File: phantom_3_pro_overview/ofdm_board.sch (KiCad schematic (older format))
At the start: 0 parts

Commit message: Overview: Conceptual schematics of some components.
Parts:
- added U?: STM32F 103CBU6, ARM Cortex-M3 MCU, symbol IC_PQFP32
- added U?: AD9363, RF 2x2 transceiver, symbol IC_PQFP32
- added U?: 5CEFA4U19I7, Altera Cyclone V FPGA, symbol IC_PQFP32
- added U?: CY7C68013A, Hi-Speed USB Ctrl., symbol CY7C420
- added U?: MGA-22003, 2.3-2.7 GHz Pwr Amp, symbol AMP
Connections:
- net labels added: GND, VCC
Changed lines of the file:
@@
 LIBS:valves
 LIBS:motors
+LIBS:ic_dil_generic
+LIBS:sensors
+LIBS:u-blox
+LIBS:amplifiers
 LIBS:phantom_3_pro_overview-cache
 EELAYER 25 0
@@
 encoding utf-8
 Sheet 2 23
-Title ""
+Title "Overview of the Phantom 3 Pro OFDM board"
 Date ""
 Rev ""
 Comp ""
-Comment1 ""
+Comment1 "This schematic does not aim to be electrically correct, it is conceptual."
 Comment2 ""
 Comment3 ""
@@
 RIB_OFDM
 Wire Bus Line
-	3100 2450 3600 2450
-Text HLabel 3600 2450 2    60   BiDi ~ 0
+	8500 1850 9000 1850
+Text HLabel 9000 1850 2    60   BiDi ~ 0
 ANTENNA1
 Wire Bus Line
-	3100 2700 3600 2700
-Text HLabel 3600 2700 2    60   BiDi ~ 0
+	8500 2100 9000 2100
+Text HLabel 9000 2100 2    60   BiDi ~ 0
 ANTENNA2
 Wire Bus Line
-	3150 2900 3650 2900
-Text HLabel 3650 2900 2    60   BiDi ~ 0
+	8550 2300 9050 2300
+Text HLabel 9050 2300 2    60   BiDi ~ 0
 ANTENNA3
 Wire Bus Line
-	3150 3100 3650 3100
-Text HLabel 3650 3100 2    60   BiDi ~ 0
+	8550 2500 9050 2500
+Text HLabel 9050 2500 2    60   BiDi ~ 0
 ANTENNA4
+$Comp
+L IC_PQFP32 U?
+U 1 1 596EF58E
+P 4050 3650
+F 0 "U?" H 4050 3550 50  0001 C CNN
+F 1 "STM32F 103CBU6" H 4050 3750 50  0000 C CNN
+F 2 "ARM Cortex-M3 MCU" H 4050 3650 50  0000 C CNN
+F 3 "DOCUMENTATION" H 4050 3650 50  0001 C CNN
+	1    4050 3650
+	1    0    0    -1
+$EndComp
+$Comp
+L IC_PQFP32 U?
+U 1 1 596EF5FD
+P 6500 2150
+F 0 "U?" H 6500 2050 50  0001 C CNN
+F 1 "AD9363" H 6500 2250 50  0000 C CNN
+F 2 "RF 2x2 transceiver" H 6500 2150 50  0000 C CNN
+F 3 "DOCUMENTATION" H 6500 2150 50  0001 C CNN
+	1    6500 2150
+	1    0    0    -1
+$EndComp
+$Comp
+L IC_PQFP32 U?
+U 1 1 596EF87B
+P 8200 4850
+F 0 "U?" H 8200 4750 50  0001 C CNN
+F 1 "5CEFA4U19I7" H 8200 4950 50  0000 C CNN
+F 2 "Altera Cyclone V FPGA" H 8200 4850 50  0000 C CNN
+F 3 "DOCUMENTATION" H 8200 4850 50  0001 C CNN
+	1    8200 4850
+	1    0    0    -1
+$EndComp
+$Comp
+L CY7C420 U?
+U 1 1 596EFA52
+P 2050 4250
+F 0 "U?" H 1500 5150 50  0001 L CNN
+F 1 "CY7C68013A" H 2350 5150 50  0000 L CNN
+F 2 "Hi-Speed USB Ctrl." H 2050 4250 50  0000 C CNN
+F 3 "" H 2050 4250 50  0001 C CNN
+	1    2050 4250
+	1    0    0    -1
+$EndComp
+$Comp
+L AMP U?
+U 1 1 596EFDFE
+P 7900 1850
+F 0 "U?" H 8150 1950 50  0001 C CNN
+F 1 "MGA-22003" H 8000 1750 50  0000 C CNN
+F 2 "2.3-2.7 GHz Pwr Amp" H 8100 1700 50  0000 C CNN
+F 3 "" H 7900 1850 50  0001 C CNN
+	1    7900 1850
+	1    0    0    -1
+$EndComp
+$Comp
+L VCC #PWR?
+U 1 1 596F00EB
+P 7800 1550
+F 0 "#PWR?" H 7800 1400 50  0001 C CNN
+F 1 "VCC" H 7800 1700 50  0000 C CNN
+F 2 "" H 7800 1550 50  0001 C CNN
+F 3 "" H 7800 1550 50  0001 C CNN
+	1    7800 1550
+	1    0    0    -1
+$EndComp
+$Comp
+L GND #PWR?
+U 1 1 596F00FF
+P 7800 2150
+F 0 "#PWR?" H 7800 1900 50  0001 C CNN
+F 1 "GND" H 7800 2000 50  0000 C CNN
+F 2 "" H 7800 2150 50  0001 C CNN
+F 3 "" H 7800 2150 50  0001 C CNN
+	1    7800 2150
+	1    0    0    -1
+$EndComp
 $EndSCHEMATC

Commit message: Overview: Added OFDM board.
Besides drawing the OFDM, components were updated.
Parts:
- removed U?: 5CEFA4U19I7, Altera Cyclone V FPGA, symbol IC_PQFP32
- removed U?: CY7C68013A, Hi-Speed USB Ctrl., symbol CY7C420
- added U? (x2): S20, Rx_Tx_switch, symbol S20
- added U? (x2): TQP3M9037, Low Noise Amp, symbol AMP
- added U? (x2): S20, Ant_select, symbol S20
- added U?: MGA-22003, 2.3-2.7 GHz Pwr Amp, symbol AMP
- added U?: CY7C68013A, Hi-Speed, symbol IC_DIL16
- added U?: 5CEFA4U19I7, Altera Cyclone V FPGA, symbol IC_PQFP48
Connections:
- wire segments 0 -> 158

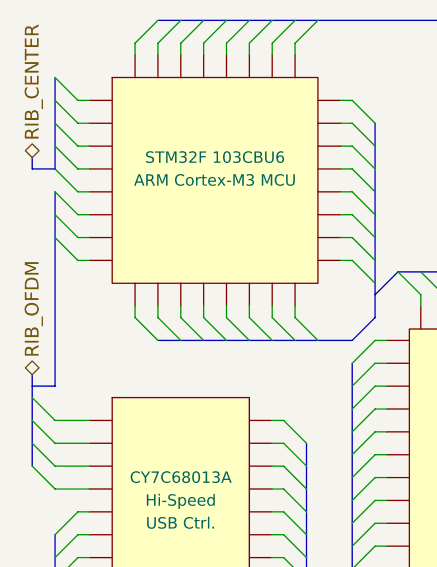
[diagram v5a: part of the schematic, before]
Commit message: Overview: Updated to latest findings.
Added magnetometer to gimbal control, and made some minor fixes.
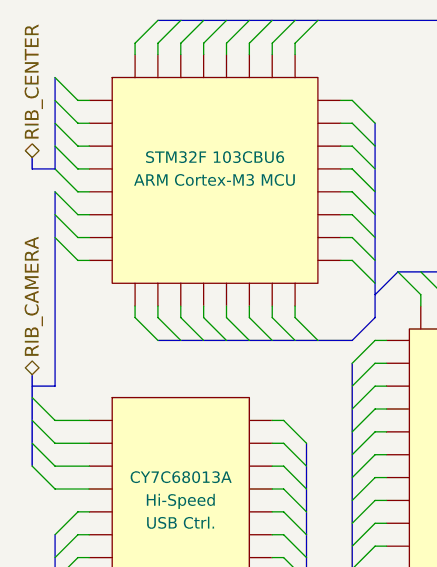
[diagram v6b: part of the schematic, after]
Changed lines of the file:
@@
 RIB_CENTER
 Text HLabel 600  2150 1    60   BiDi ~ 0
-RIB_OFDM
+RIB_CAMERA
 Text HLabel 8350 1900 2    60   BiDi ~ 0
 ANTENNA1

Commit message: Overview: Upgraded to KiCAD 5.0.1.
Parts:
- U? (x2): symbol IC_PQFP32 -> ic_dil_generic:IC_PQFP32
- U? (x4): symbol AMP -> amplifiers:AMP
- U? (x4): symbol S20 -> transistors-switches:S20
- U?: symbol IC_DIL16 -> ic_dil_generic:IC_DIL16
- U?: symbol IC_PQFP48 -> ic_dil_generic:IC_PQFP48
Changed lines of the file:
@@
-EESchema Schematic File Version 2
-LIBS:power
-LIBS:device
-LIBS:transistors
-LIBS:conn
-LIBS:linear
-LIBS:regul
-LIBS:74xx
-LIBS:cmos4000
-LIBS:adc-dac
-LIBS:memory
-LIBS:xilinx
-LIBS:microcontrollers
-LIBS:dsp
-LIBS:microchip
-LIBS:analog_switches
-LIBS:motorola
-LIBS:texas
-LIBS:intel
-LIBS:audio
-LIBS:interface
-LIBS:digital-audio
-LIBS:philips
-LIBS:display
-LIBS:cypress
-LIBS:siliconi
-LIBS:opto
-LIBS:atmel
-LIBS:contrib
-LIBS:valves
-LIBS:motors
-LIBS:ic_dil_generic
-LIBS:sensors
-LIBS:u-blox
-LIBS:amplifiers
-LIBS:transistors-switches
-LIBS:transistors-power
-LIBS:sensors-v2
-LIBS:regul-v2
+EESchema Schematic File Version 4
 LIBS:phantom_3_pro_overview-cache
-EELAYER 25 0
+EELAYER 26 0
 EELAYER END
 $Descr User 9449 5276
@@
 ANTENNA4
 $Comp
-L IC_PQFP32 U?
+L ic_dil_generic:IC_PQFP32 U?
 U 1 1 596EF58E
 P 1400 1300
@@
 $EndComp
 $Comp
-L IC_PQFP32 U?
+L ic_dil_generic:IC_PQFP32 U?
 U 1 1 596EF5FD
 P 4600 2700
@@
 $EndComp
 $Comp
-L AMP U?
+L amplifiers:AMP U?
 U 1 1 596EFDFE
 P 6350 1500
@@
 $EndComp
 $Comp
-L VCC #PWR?
+L power:VCC #PWR?
 U 1 1 596F00EB
 P 6250 1200
@@
 $EndComp
 $Comp
-L GND #PWR?
+L power:GND #PWR?
 U 1 1 596F00FF
 P 6250 1800
@@
 $EndComp
 $Comp
-L S20 U?
+L transistors-switches:S20 U?
 U 1 1 596FC8A9
 P 6950 2000
@@
 $EndComp
 $Comp
-L AMP U?
+L amplifiers:AMP U?
 U 1 1 596FC948
 P 5950 2000
@@
 $EndComp
 $Comp
-L VCC #PWR?
+L power:VCC #PWR?
 U 1 1 596FC94E
 P 6050 1700
@@
 $EndComp
 $Comp
-L GND #PWR?
+L power:GND #PWR?
 U 1 1 596FC954
 P 6050 2300
@@
 $EndComp
 $Comp
-L S20 U?
+L transistors-switches:S20 U?
 U 1 1 596FCA38
 P 7700 2000
@@
 $EndComp
 $Comp
-L VCC #PWR?
+L power:VCC #PWR?
 U 1 1 596FCA54
 P 6650 2300
@@
 $EndComp
 $Comp
-L VCC #PWR?
+L power:VCC #PWR?
 U 1 1 596FCA5F
 P 7700 1700
@@
 $EndComp
 $Comp
-L GND #PWR?
+L power:GND #PWR?
 U 1 1 596FCA6A
 P 7050 1600
@@
 $EndComp
 $Comp
-L GND #PWR?
+L power:GND #PWR?
 U 1 1 596FCA75
 P 7700 2300
@@
 	8050 2100 8150 2200
 $Comp
-L GND #PWR?
+L power:GND #PWR?
 U 1 1 596FCB1A
 P 8300 2000
@@
 	8150 2100 8250 2200
 $Comp
-L AMP U?
+L amplifiers:AMP U?
 U 1 1 596FD101
 P 6350 2550
@@
 $EndComp
 $Comp
-L VCC #PWR?
+L power:VCC #PWR?
 U 1 1 596FD107
 P 6250 2250
@@
 $EndComp
 $Comp
-L GND #PWR?
+L power:GND #PWR?
 U 1 1 596FD10D
 P 6250 2850
@@
 $EndComp
 $Comp
-L S20 U?
+L transistors-switches:S20 U?
 U 1 1 596FD113
 P 6950 3050
@@
 $EndComp
 $Comp
-L AMP U?
+L amplifiers:AMP U?
 U 1 1 596FD119
 P 5950 3050
@@
 $EndComp
 $Comp
-L VCC #PWR?
+L power:VCC #PWR?
 U 1 1 596FD11F
 P 6050 2750
@@
 $EndComp
 $Comp
-L GND #PWR?
+L power:GND #PWR?
 U 1 1 596FD125
 P 6050 3350
@@
 $EndComp
 $Comp
-L S20 U?
+L transistors-switches:S20 U?
 U 1 1 596FD12D
 P 7700 3050
@@
 $EndComp
 $Comp
-L VCC #PWR?
+L power:VCC #PWR?
 U 1 1 596FD133
 P 6650 3350
@@
 $EndComp
 $Comp
-L VCC #PWR?
+L power:VCC #PWR?
 U 1 1 596FD139
 P 7700 2750
@@
 $EndComp
 $Comp
-L GND #PWR?
+L power:GND #PWR?
 U 1 1 596FD13F
 P 7050 2650
@@
 $EndComp
 $Comp
-L GND #PWR?
+L power:GND #PWR?
 U 1 1 596FD145
 P 7700 3350
@@
 	8050 3150 8150 3250
 $Comp
-L GND #PWR?
+L power:GND #PWR?
 U 1 1 596FD153
 P 8300 3050
@@
 	8150 3150 8250 3250
 $Comp
-L IC_DIL16 U?
+L ic_dil_generic:IC_DIL16 U?
 U 1 1 596FEAF5
 P 1250 2700
@@
 	4950 2150 4950 2100
 $Comp
-L IC_PQFP48 U?
+L ic_dil_generic:IC_PQFP48 U?
 U 1 1 59703C40
 P 2850 2550
